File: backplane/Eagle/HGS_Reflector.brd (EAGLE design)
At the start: 100 x 100 mm, 0 parts

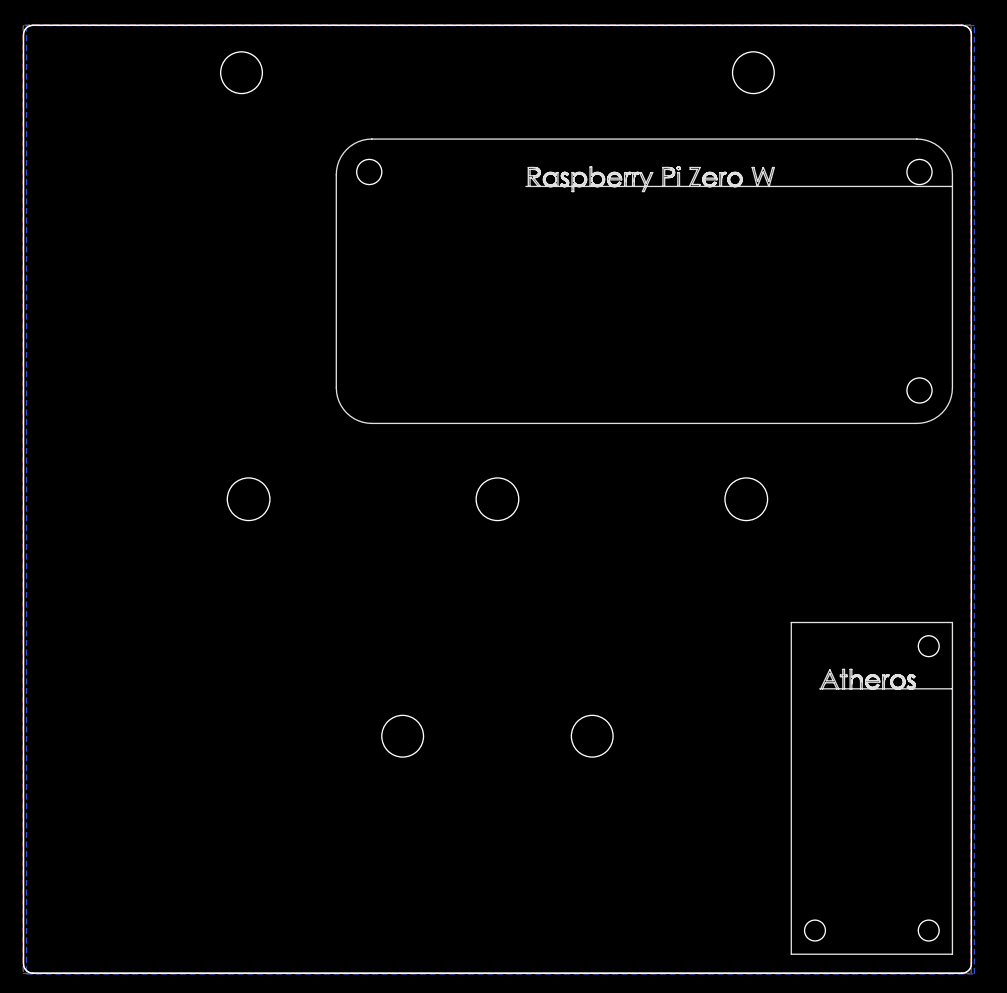
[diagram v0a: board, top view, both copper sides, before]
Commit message: handheld ground station eagle mockup
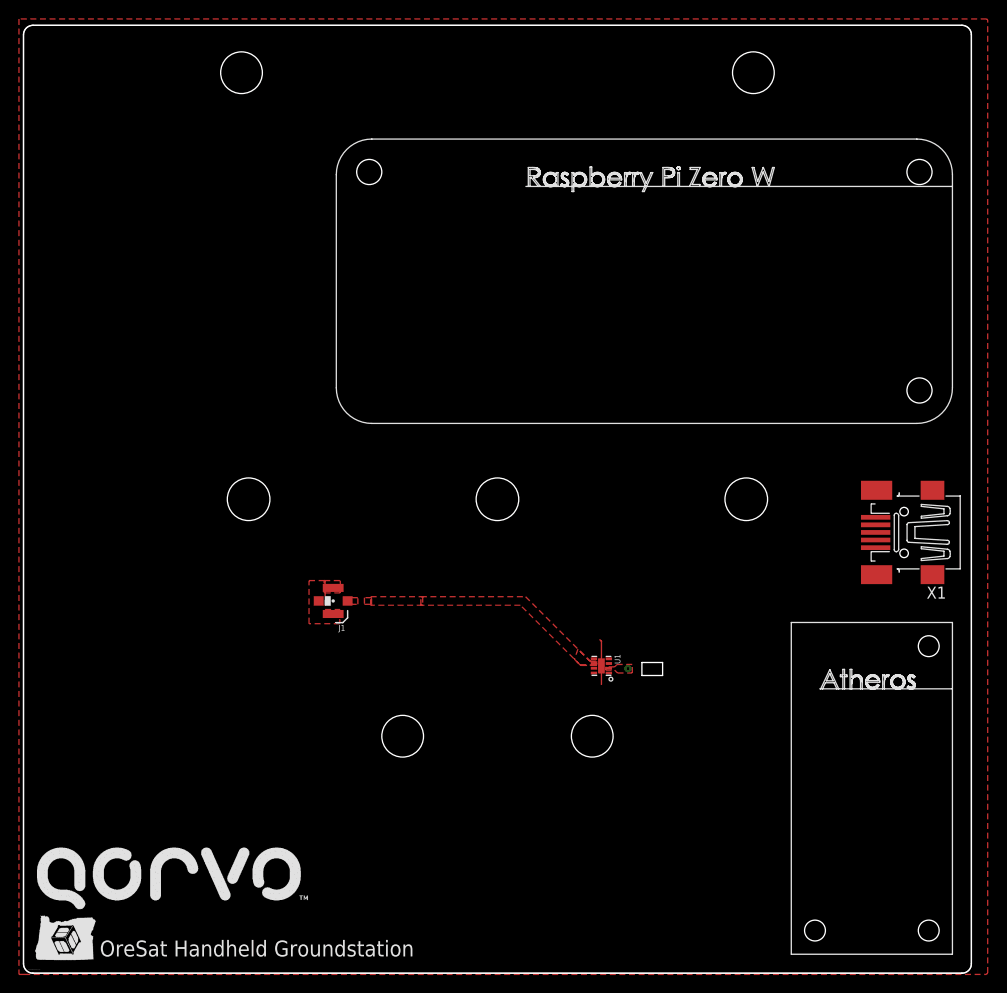
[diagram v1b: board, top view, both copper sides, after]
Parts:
- added J1: U.FL, SparkFun-Connectors:U.FL
- added U1: TQP3M9037, U-Qorvo-TQP3M9037-LNA:DFN8-2X2-WITH-PAD
- added X1: MINI-USB-32005-201, con-cypressindustries:32005-201
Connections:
- new net GND: J1.1, J1.2, J1.FEED, U1.PAD
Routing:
- net GND: track 0.00 -> 4.76 mm
- added copper zone on layer 1, net N$1
- added copper zone on layer 1, net N$3
- added copper zone on layer 1, net N$4
- removed copper zone on layer 16, net GND
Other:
- outline, holes or cut-outs redrawn
- board text added: "C:/Users/dal56/Downloads/qorvo (1).bmp"
- board text added: "OreSat Handheld Groundstation"
